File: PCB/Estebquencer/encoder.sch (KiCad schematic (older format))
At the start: 1 part

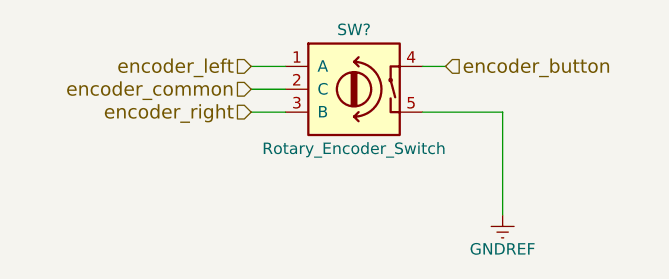
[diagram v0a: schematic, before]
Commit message: se arregló cableado encoder
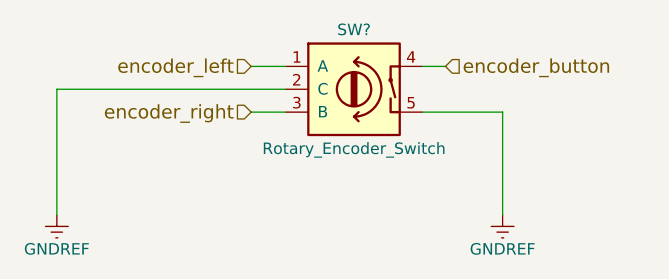
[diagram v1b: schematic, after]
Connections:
- net encoder_common is gone; now on net GNDREF: SW?.2 (C)
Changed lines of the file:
@@
 Text HLabel 5400 3450 0    60   Input ~ 0
 encoder_left
-Text HLabel 5400 3550 0    60   Input ~ 0
-encoder_common
 Text HLabel 5400 3650 0    60   Input ~ 0
 encoder_right
@@
 	5400 3450 5550 3450
 Wire Wire Line
-	5400 3550 5550 3550
+	4550 3550 5550 3550
 Wire Wire Line
 	5550 3650 5400 3650
+$Comp
+L GNDREF #PWR?
+U 1 1 58736298
+P 4550 4100
+F 0 "#PWR?" H 4550 3850 50  0001 C CNN
+F 1 "GNDREF" H 4550 3950 50  0000 C CNN
+F 2 "" H 4550 4100 50  0000 C CNN
+F 3 "" H 4550 4100 50  0000 C CNN
+	1    4550 4100
+	1    0    0    -1
+$EndComp
+Wire Wire Line
+	4550 3550 4550 4100
 $EndSCHEMATC
